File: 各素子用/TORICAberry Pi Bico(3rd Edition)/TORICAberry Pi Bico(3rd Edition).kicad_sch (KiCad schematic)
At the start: 46 parts, among them J1 USB_C_Receptacle, J2 Conn_01x08_Socket, J5 Conn_01x11_Socket, SW1 SW_Push, SW2 SW_Push, U1 RP2040, U3 NCP1117-3.3_TO252, Y1 Crystal_GND24

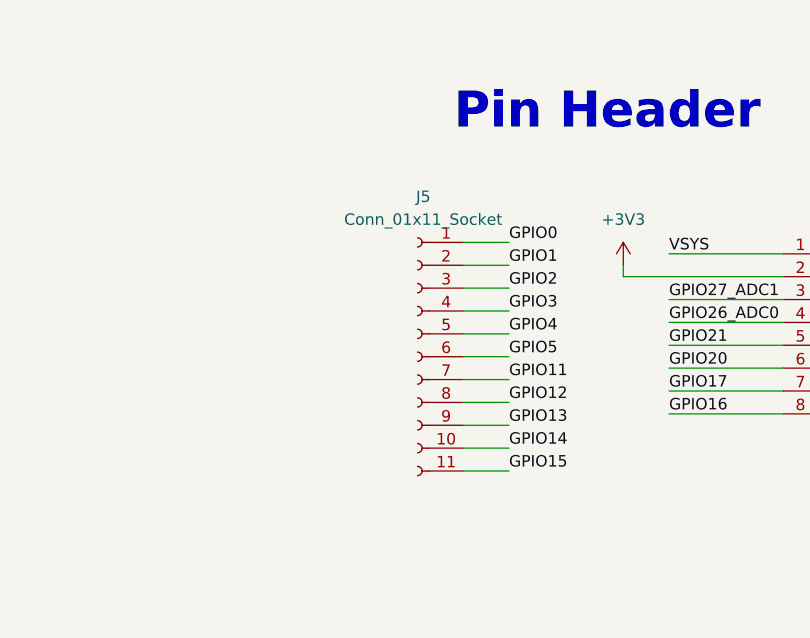
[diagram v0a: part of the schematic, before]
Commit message: RX-ESP delete
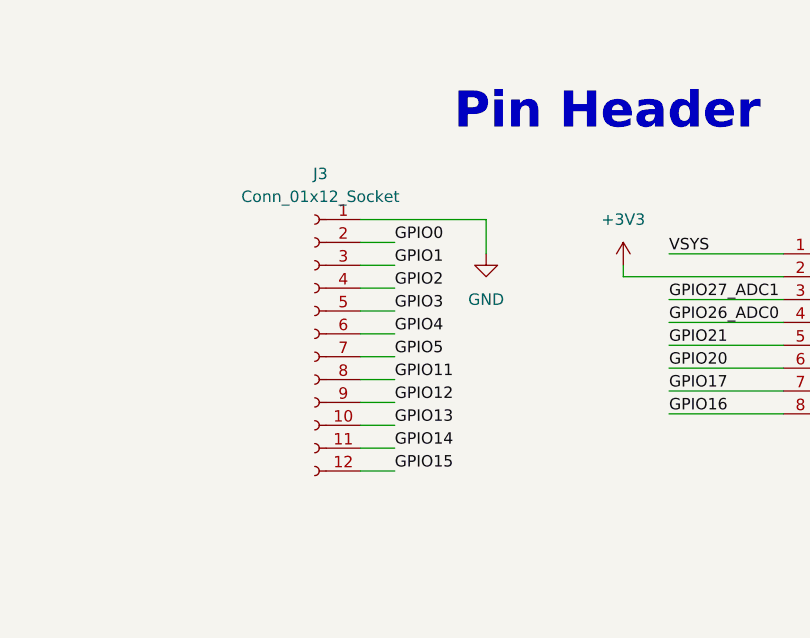
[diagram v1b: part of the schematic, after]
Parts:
- removed J5: Conn_01x11_Socket, Connector_PinHeader_2.54mm:PinHeader_1x11_P2.54mm_Vertical, symbol Connector:Conn_01x11_Socket
- added J3: Conn_01x12_Socket, Connector_PinHeader_2.54mm:PinHeader_1x12_P2.54mm_Vertical, symbol Connector:Conn_01x12_Socket
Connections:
- net GND: now also J3.1 (Pin_1)
- net GPIO0: now also J3.2 (Pin_2)
- net GPIO1: now also J3.3 (Pin_3)
- net GPIO11: now also J3.8 (Pin_8)
- net GPIO12: now also J3.9 (Pin_9)
- net GPIO13: now also J3.10 (Pin_10)
- net GPIO14: now also J3.11 (Pin_11)
- net GPIO15: now also J3.12 (Pin_12)
- net GPIO2: now also J3.4 (Pin_4)
- net GPIO3: now also J3.5 (Pin_5)
- net GPIO4: now also J3.6 (Pin_6)
- net GPIO5: now also J3.7 (Pin_7)
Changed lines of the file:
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@@
 	(wire
 		(pts
-			(xy 368.3 119.38) (xy 373.38 119.38)
+			(xy 356.87 119.38) (xy 360.68 119.38)
 		)
 		(stroke
@@
 	(wire
 		(pts
-			(xy 368.3 121.92) (xy 373.38 121.92)
+			(xy 356.87 121.92) (xy 360.68 121.92)
 		)
 		(stroke
@@
 	(wire
 		(pts
-			(xy 368.3 114.3) (xy 373.38 114.3)
+			(xy 356.87 114.3) (xy 360.68 114.3)
 		)
 		(stroke
@@
 	(wire
 		(pts
+			(xy 370.84 104.14) (xy 370.84 107.95)
+		)
+		(stroke
+			(width 0)
+			(type default)
+		)
+	)
+	(wire
+		(pts
 			(xy 91.44 107.95) (xy 102.87 107.95)
 		)
@@
 	(wire
 		(pts
-			(xy 368.3 132.08) (xy 373.38 132.08)
+			(xy 356.87 132.08) (xy 360.68 132.08)
 		)
 		(stroke
@@
 	(wire
 		(pts
-			(xy 368.3 127) (xy 373.38 127)
+			(xy 356.87 127) (xy 360.68 127)
 		)
 		(stroke
@@
 	(wire
 		(pts
-			(xy 368.3 109.22) (xy 373.38 109.22)
+			(xy 356.87 109.22) (xy 360.68 109.22)
 		)
 		(stroke
@@
 	(wire
 		(pts
-			(xy 368.3 116.84) (xy 373.38 116.84)
+			(xy 356.87 116.84) (xy 360.68 116.84)
 		)
 		(stroke
@@
 	(wire
 		(pts
-			(xy 368.3 106.68) (xy 373.38 106.68)
+			(xy 356.87 106.68) (xy 360.68 106.68)
 		)
 		(stroke
@@
 	(wire
 		(pts
+			(xy 356.87 104.14) (xy 370.84 104.14)
+		)
+		(stroke
+			(width 0)
+			(type default)
+		)
+	)
+	(wire
+		(pts
 			(xy 46.99 77.47) (xy 46.99 74.93)
 		)
@@
 	(wire
 		(pts
-			(xy 368.3 124.46) (xy 373.38 124.46)
+			(xy 356.87 124.46) (xy 360.68 124.46)
 		)
 		(stroke
@@
 	(wire
 		(pts
-			(xy 368.3 129.54) (xy 373.38 129.54)
+			(xy 356.87 129.54) (xy 360.68 129.54)
 		)
 		(stroke
@@
 	(wire
 		(pts
-			(xy 368.3 111.76) (xy 373.38 111.76)
+			(xy 356.87 111.76) (xy 360.68 111.76)
 		)
 		(stroke
@@
 	)
 	(label "GPIO0"
-		(at 373.38 106.68 0)
+		(at 360.68 106.68 0)
 		(effects
 			(font
@@
 	)
 	(label "GPIO2"
-		(at 373.38 111.76 0)
+		(at 360.68 111.76 0)
 		(effects
 			(font
@@
 	)
 	(label "GPIO3"
-		(at 373.38 114.3 0)
+		(at 360.68 114.3 0)
 		(effects
 			(font
@@
 	)
 	(label "GPIO11"
-		(at 373.38 121.92 0)
+		(at 360.68 121.92 0)
 		(effects
 			(font
@@
 	)
 	(label "GPIO15"
-		(at 373.38 132.08 0)
+		(at 360.68 132.08 0)
 		(effects
 			(font
@@
 	)
 	(label "GPIO14"
-		(at 373.38 129.54 0)
+		(at 360.68 129.54 0)
 		(effects
 			(font
@@
 	)
 	(label "GPIO13"
-		(at 373.38 127 0)
+		(at 360.68 127 0)
 		(effects
 			(font
@@
 	)
 	(label "GPIO4"
-		(at 373.38 116.84 0)
+		(at 360.68 116.84 0)
 		(effects
 			(font
@@
 	)
 	(label "GPIO1"
-		(at 373.38 109.22 0)
+		(at 360.68 109.22 0)
 		(effects
 			(font
@@
 	)
 	(label "GPIO12"
-		(at 373.38 124.46 0)
+		(at 360.68 124.46 0)
 		(effects
 			(font
@@
 	)
 	(label "GPIO5"
-		(at 373.38 119.38 0)
+		(at 360.68 119.38 0)
 		(effects
 			(font
@@
 	)
 	(symbol
+		(lib_id "power:GND")
+		(at 370.84 107.95 0)
+		(unit 1)
+		(exclude_from_sim no)
+		(in_bom yes)
+		(on_board yes)
+		(dnp no)
+		(fields_autoplaced yes)
+		(property "Reference" "#PWR033"
+			(at 370.84 114.3 0)
+			(effects
+				(font
+					(size 1.27 1.27)
+				)
+				(hide yes)
+			)
+		)
+		(property "Value" "GND"
+			(at 370.84 113.03 0)
+			(effects
+				(font
+					(size 1.27 1.27)
+				)
+			)
+		)
+		(property "Footprint" ""
+			(at 370.84 107.95 0)
+			(effects
+				(font
+					(size 1.27 1.27)
+				)
+				(hide yes)
+			)
+		)
+		(property "Datasheet" ""
+			(at 370.84 107.95 0)
+			(effects
+				(font
+					(size 1.27 1.27)
+				)
+				(hide yes)
+			)
+		)
+		(property "Description" "Power symbol creates a global label with name \"GND\" , ground"
+			(at 370.84 107.95 0)
+			(effects
+				(font
+					(size 1.27 1.27)
+				)
+				(hide yes)
+			)
+		)
+		(pin "1"
+		)
+		(instances
+			(project ""
+				(path "/c3225fe2-8897-4cd6-b019-d43b32d88a89"
+					(reference "#PWR033")
+					(unit 1)
+				)
+			)
+		)
+	)
+	(symbol
 		(lib_id "MCU_RaspberryPi:RP2040")
 		(at 66.04 123.19 0)
@@
 	)
 	(symbol
-		(lib_id "Connector:Conn_01x11_Socket")
-		(at 363.22 119.38 0)
+		(lib_id "Connector:Conn_01x12_Socket")
+		(at 351.79 116.84 0)
 		(mirror y)
 		(unit 1)
@@
 		(dnp no)
 		(fields_autoplaced yes)
-		(property "Reference" "J5"
-			(at 363.855 101.6 0)
+		(property "Reference" "J3"
+			(at 352.425 99.06 0)
 			(effects
 				(font
@@
 			)
 		)
-		(property "Value" "Conn_01x11_Socket"
-			(at 363.855 104.14 0)
+		(property "Value" "Conn_01x12_Socket"
+			(at 352.425 101.6 0)
 			(effects
 				(font
@@
 			)
 		)
-		(property "Footprint" "Connector_PinHeader_2.54mm:PinHeader_1x11_P2.54mm_Vertical"
-			(at 363.22 119.38 0)
+		(property "Footprint" "Connector_PinHeader_2.54mm:PinHeader_1x12_P2.54mm_Vertical"
+			(at 351.79 116.84 0)
 			(effects
 				(font
@@
 		)
 		(property "Datasheet" "~"
-			(at 363.22 119.38 0)
+			(at 351.79 116.84 0)
 			(effects
 				(font
@@
 			)
 		)
-		(property "Description" "Generic connector, single row, 01x11, script generated"
-			(at 363.22 119.38 0)
+		(property "Description" "Generic connector, single row, 01x12, script generated"
+			(at 351.79 116.84 0)
 			(effects
 				(font
@@
 			)
 		)
-		(pin "1"
+		(pin "11"
+		)
+		(pin "5"
+		)
+		(pin "8"
 		)
 		(pin "2"
 		)
-		(pin "4"
+		(pin "9"
 		)
-		(pin "10"
+		(pin "1"
 		)
-		(pin "5"
+		(pin "12"
 		)
-		(pin "3"
+		(pin "10"
 		)
-		(pin "6"
+		(pin "3"
 		)
 		(pin "7"
 		)
-		(pin "8"
-		)
-		(pin "9"
+		(pin "4"
 		)
-		(pin "11"
+		(pin "6"
 		)
 		(instances
 			(project ""
 				(path "/c3225fe2-8897-4cd6-b019-d43b32d88a89"
-					(reference "J5")
+					(reference "J3")
 					(unit 1)
 				)
